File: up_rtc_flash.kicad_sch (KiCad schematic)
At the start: 12 parts, among them IC202 PCF8563T_5,518, IC203 W25Q128JVSIQTR, X201 PCIE-52P40H, X202 32.768 kHz, X203 TF-15×15, X204 CR1220-2ZX

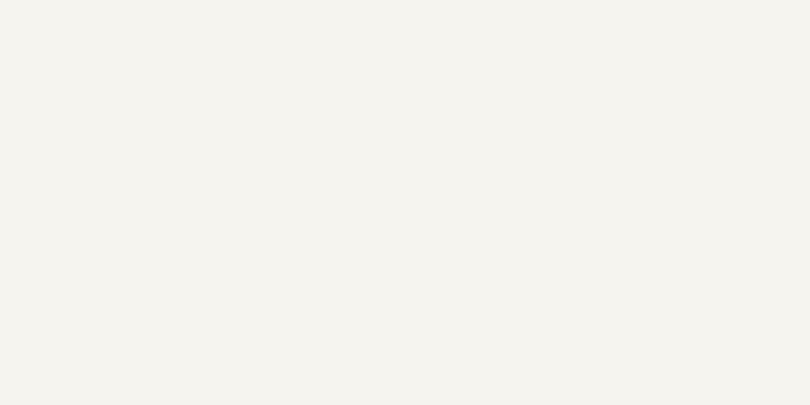
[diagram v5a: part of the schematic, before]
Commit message: add I2C0 Pullups
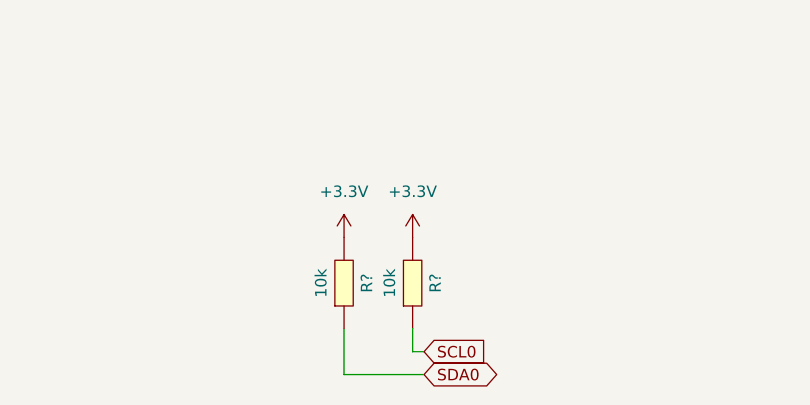
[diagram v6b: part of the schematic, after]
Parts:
- added R? (x2): 10k, R0402, symbol eduboardv2:0402WGF100JTCE
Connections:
- net SCL0: now also R?.1
- net SDA0: now also R?.1
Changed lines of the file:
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@@
   (junction (at 240.03 64.77) (diameter 0) (color 0 0 0 0)
   )
+  (wire (pts (xy 162.56 190.5) (xy 163.83 190.5))
+    (stroke (width 0) (type default) (color 0 0 0 0))
+  )
   (wire (pts (xy 168.91 39.37) (xy 171.45 39.37))
     (stroke (width 0) (type default) (color 0 0 0 0))
   )
+  (wire (pts (xy 154.94 193.04) (xy 163.83 193.04))
+    (stroke (width 0) (type default) (color 0 0 0 0))
+  )
   (wire (pts (xy 217.17 39.37) (xy 236.22 39.37))
     (stroke (width 0) (type default) (color 0 0 0 0))
@@
     (stroke (width 0) (type default) (color 0 0 0 0))
   )
+  (wire (pts (xy 162.56 187.96) (xy 162.56 190.5))
+    (stroke (width 0) (type default) (color 0 0 0 0))
+  )
   (wire (pts (xy 171.45 39.37) (xy 189.23 39.37))
     (stroke (width 0) (type default) (color 0 0 0 0))
@@
   )
   (wire (pts (xy 252.73 44.45) (xy 252.73 39.37))
+    (stroke (width 0) (type default) (color 0 0 0 0))
+  )
+  (wire (pts (xy 154.94 187.96) (xy 154.94 193.04))
     (stroke (width 0) (type default) (color 0 0 0 0))
   )
@@
     )
   )
+  (global_label "SDA0" (shape bidirectional) (at 163.83 193.04 0) (fields_autoplaced)
+    (effects (font (size 1.27 1.27)) (justify left))
+    (property "Intersheet References" "${INTERSHEET_REFS}" (id 0) (at 171.0207 192.9606 0)
+      (effects (font (size 1.27 1.27)) (justify left) hide)
+    )
+  )
+  (global_label "SCL0" (shape input) (at 163.83 190.5 0) (fields_autoplaced)
+    (effects (font (size 1.27 1.27)) (justify left))
+    (property "Intersheet References" "${INTERSHEET_REFS}" (id 0) (at 170.9602 190.4206 0)
+      (effects (font (size 1.27 1.27)) (justify left) hide)
+    )
+  )
   (global_label "RTC_INT" (shape output) (at 189.23 44.45 180) (fields_autoplaced)
     (effects (font (size 1.27 1.27)) (justify right))
@@
     (pin "1")
     (pin "2")
+  )
+  (symbol (lib_name "+3.3V_2") (lib_id "eduboardv2:+3.3V") (at 154.94 177.8 0) (unit 1)
+    (in_bom yes) (on_board yes) (fields_autoplaced)
+    (property "Reference" "#PWR?" (id 0) (at 154.94 181.61 0)
+      (effects (font (size 1.27 1.27)) hide)
+    )
+    (property "Value" "+3.3V" (id 1) (at 154.94 172.72 0))
+    (property "Footprint" "" (id 2) (at 154.94 177.8 0)
+      (effects (font (size 1.27 1.27)) hide)
+    )
+    (property "Datasheet" "" (id 3) (at 154.94 177.8 0)
+      (effects (font (size 1.27 1.27)) hide)
+    )
+    (pin "1")
   )
   (symbol (lib_name "GND_6") (lib_id "eduboardv2:GND") (at 220.98 133.35 270) (unit 1)
@@
     )
     (pin "1")
+  )
+  (symbol (lib_name "0402WGF100JTCE_10") (lib_id "eduboardv2:0402WGF100JTCE") (at 154.94 182.88 90) (unit 1)
+    (in_bom yes) (on_board yes)
+    (property "Reference" "R?" (id 0) (at 157.48 182.88 0))
+    (property "Value" "10k" (id 1) (at 152.4 182.88 0))
+    (property "Footprint" "R0402" (id 2) (at 162.56 182.88 0)
+      (effects (font (size 1.27 1.27)) hide)
+    )
+    (property "Datasheet" "https://lcsc.com/product-detail/Chip-Resistor-Surface-Mount-UniOhm_10R-10R0-1_C25077.html" (id 3) (at 167.64 182.88 0)
+      (effects (font (size 1.27 1.27)) hide)
+    )
+    (property "Manufacturer" "UniOhm" (id 4) (at 170.18 182.88 0)
+      (effects (font (size 1.27 1.27)) hide)
+    )
+    (property "LCSC Part" "C25077" (id 5) (at 172.72 182.88 0)
+      (effects (font (size 1.27 1.27)) hide)
+    )
+    (property "JLC Part" "Basic Part" (id 6) (at 175.26 182.88 0)
+      (effects (font (size 1.27 1.27)) hide)
+    )
+    (property "MPN" "0402WGF100JTCE" (id 7) (at 160.02 182.88 0)
+      (effects (font (size 1.27 1.27)) hide)
+    )
+    (pin "1")
+    (pin "2")
   )
   (symbol (lib_id "eduboardv2:+3.3V") (at 195.58 123.19 0) (unit 1)
@@
     (pin "9")
   )
+  (symbol (lib_name "0402WGF100JTCE_10") (lib_id "eduboardv2:0402WGF100JTCE") (at 162.56 182.88 90) (unit 1)
+    (in_bom yes) (on_board yes)
+    (property "Reference" "R?" (id 0) (at 165.1 182.88 0))
+    (property "Value" "10k" (id 1) (at 160.02 182.88 0))
+    (property "Footprint" "R0402" (id 2) (at 170.18 182.88 0)
+      (effects (font (size 1.27 1.27)) hide)
+    )
+    (property "Datasheet" "https://lcsc.com/product-detail/Chip-Resistor-Surface-Mount-UniOhm_10R-10R0-1_C25077.html" (id 3) (at 175.26 182.88 0)
+      (effects (font (size 1.27 1.27)) hide)
+    )
+    (property "Manufacturer" "UniOhm" (id 4) (at 177.8 182.88 0)
+      (effects (font (size 1.27 1.27)) hide)
+    )
+    (property "LCSC Part" "C25077" (id 5) (at 180.34 182.88 0)
+      (effects (font (size 1.27 1.27)) hide)
+    )
+    (property "JLC Part" "Basic Part" (id 6) (at 182.88 182.88 0)
+      (effects (font (size 1.27 1.27)) hide)
+    )
+    (property "MPN" "0402WGF100JTCE" (id 7) (at 167.64 182.88 0)
+      (effects (font (size 1.27 1.27)) hide)
+    )
+    (pin "1")
+    (pin "2")
+  )
   (symbol (lib_name "+3.3V_2") (lib_id "eduboardv2:+3.3V") (at 236.22 26.67 0) (unit 1)
     (in_bom yes) (on_board yes) (fields_autoplaced)
@@
       (effects (font (size 1.27 1.27)) hide)
     )
+    (pin "1")
+  )
+  (symbol (lib_name "+3.3V_2") (lib_id "eduboardv2:+3.3V") (at 162.56 177.8 0) (unit 1)
+    (in_bom yes) (on_board yes) (fields_autoplaced)
+    (property "Reference" "#PWR?" (id 0) (at 162.56 181.61 0)
+      (effects (font (size 1.27 1.27)) hide)
+    )
+    (property "Value" "+3.3V" (id 1) (at 162.56 172.72 0))
+    (property "Footprint" "" (id 2) (at 162.56 177.8 0)
+      (effects (font (size 1.27 1.27)) hide)
+    )
+    (property "Datasheet" "" (id 3) (at 162.56 177.8 0)
+      (effects (font (size 1.27 1.27)) hide)
+    )

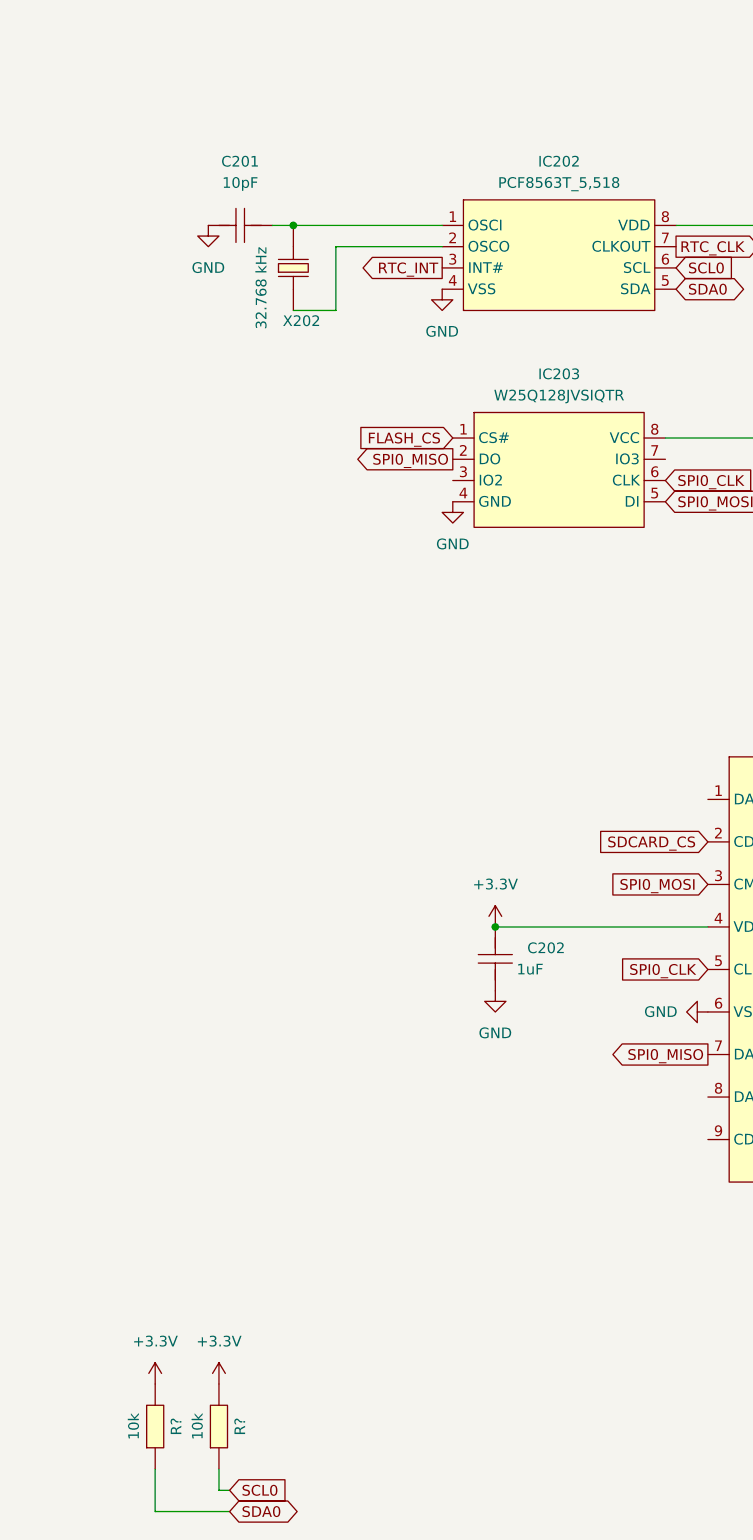
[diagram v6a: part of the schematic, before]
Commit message: reassign symbol references after page movements. Place in pcb
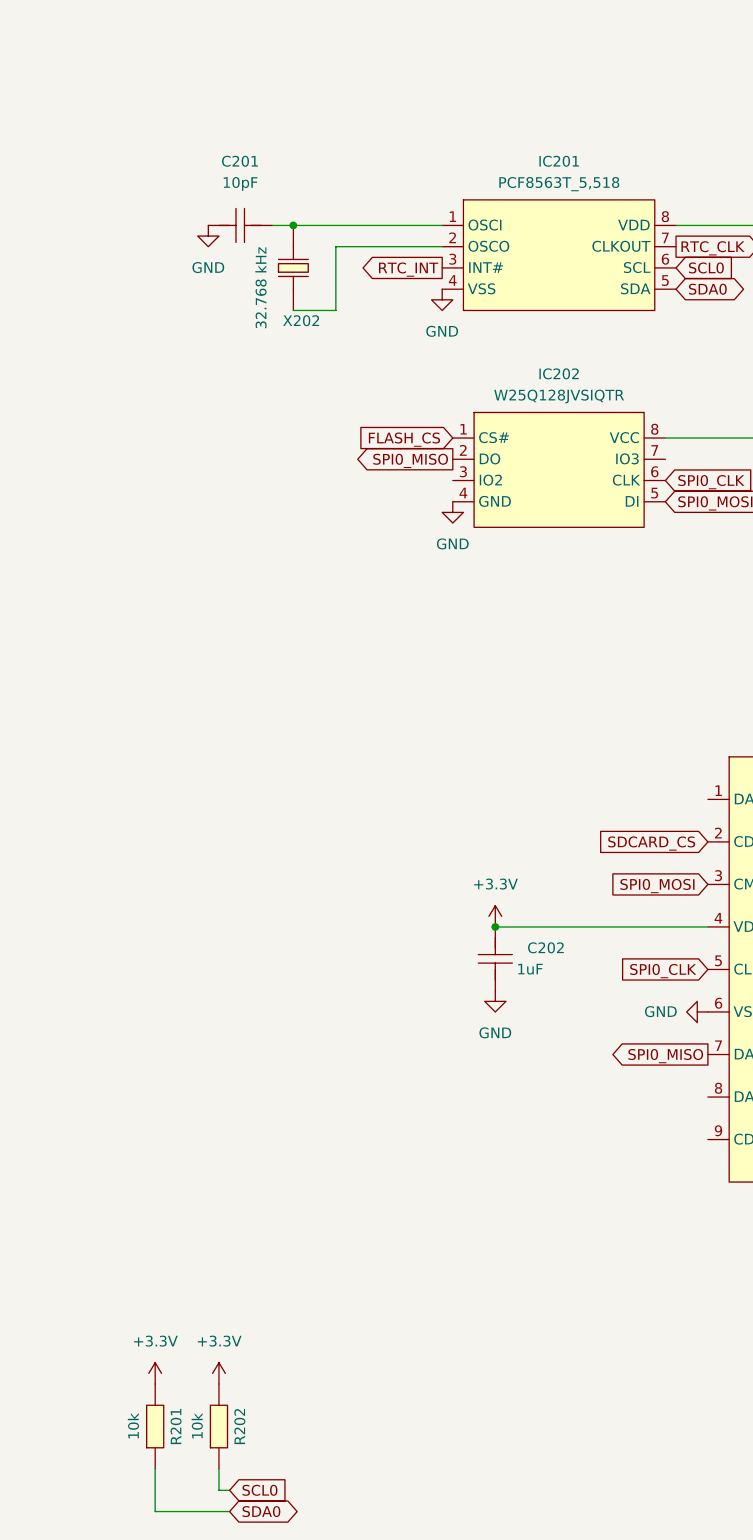
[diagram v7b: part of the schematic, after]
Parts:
- C201, C202, C203, C204: footprint C0402 -> eduboardv2:C0402
- D201, D202: footprint SOD-123_L2.7-W1.6-LS3.7-RD-1 -> eduboardv2:SOD-123_L2.7-W1.6-LS3.7-RD-1
- IC201: renamed from IC202; footprint SOIC-8_L5.0-W4.0-P1.27-LS6.0-BL -> eduboardv2:SOIC-8_L5.0-W4.0-P1.27-LS6.0-BL
- IC202: renamed from IC203; footprint SOIC-8_L5.3-W5.3-P1.27-LS8.0-BL -> eduboardv2:SOIC-8_L5.3-W5.3-P1.27-LS8.0-BL
- R201, R202: renamed from R?; footprint R0402 -> eduboardv2:R0402
- X201: footprint PCIE-SMD_PCIE-52P40H -> eduboardv2:PCIE-SMD_PCIE-52P40H
- X202: footprint FC-135R_L3.2-W1.5 -> eduboardv2:FC-135R_L3.2-W1.5
- X203: footprint TF-SMD_TF-15-15 -> eduboardv2:TF-SMD_TF-15-15
- X204: footprint BAT-SMD_CR1220-2ZX -> eduboardv2:BAT-SMD_CR1220-2ZX
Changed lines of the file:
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@@
     (property "Reference" "D202" (id 0) (at 247.269 33.02 0))
     (property "Value" "B5819W_C8598" (id 1) (at 247.269 35.56 0))
-    (property "Footprint" "SOD-123_L2.7-W1.6-LS3.7-RD-1" (id 2) (at 247.65 46.99 0)
+    (property "Footprint" "eduboardv2:SOD-123_L2.7-W1.6-LS3.7-RD-1" (id 2) (at 247.65 46.99 0)
       (effects (font (size 1.27 1.27)) hide)
     )
@@
   (symbol (lib_name "+3.3V_2") (lib_id "eduboardv2:+3.3V") (at 154.94 177.8 0) (unit 1)
     (in_bom yes) (on_board yes) (fields_autoplaced)
-    (property "Reference" "#PWR?" (id 0) (at 154.94 181.61 0)
+    (property "Reference" "#PWR0201" (id 0) (at 154.94 181.61 0)
       (effects (font (size 1.27 1.27)) hide)
     )
@@
   (symbol (lib_name "GND_6") (lib_id "eduboardv2:GND") (at 220.98 133.35 270) (unit 1)
     (in_bom yes) (on_board yes)
-    (property "Reference" "#PWR0206" (id 0) (at 214.63 133.35 0)
+    (property "Reference" "#PWR0208" (id 0) (at 214.63 133.35 0)
       (effects (font (size 1.27 1.27)) hide)
     )
@@
   (symbol (lib_id "eduboardv2:W25Q128JVSIQTR") (at 203.2 68.58 0) (unit 1)
     (in_bom yes) (on_board yes) (fields_autoplaced)
-    (property "Reference" "IC203" (id 0) (at 203.2 57.15 0))
+    (property "Reference" "IC202" (id 0) (at 203.2 57.15 0))
     (property "Value" "W25Q128JVSIQTR" (id 1) (at 203.2 59.69 0))
-    (property "Footprint" "SOIC-8_L5.3-W5.3-P1.27-LS8.0-BL" (id 2) (at 203.2 80.01 0)
+    (property "Footprint" "eduboardv2:SOIC-8_L5.3-W5.3-P1.27-LS8.0-BL" (id 2) (at 203.2 80.01 0)
       (effects (font (size 1.27 1.27)) hide)
     )
@@
   (symbol (lib_name "GND_2") (lib_id "eduboardv2:GND") (at 190.5 72.39 0) (unit 1)
     (in_bom yes) (on_board yes) (fields_autoplaced)
-    (property "Reference" "#PWR0203" (id 0) (at 190.5 78.74 0)
+    (property "Reference" "#PWR0205" (id 0) (at 190.5 78.74 0)
       (effects (font (size 1.27 1.27)) hide)
     )
@@
     (property "Reference" "C201" (id 0) (at 165.1 31.75 0))
     (property "Value" "10pF" (id 1) (at 165.1 34.29 0))
-    (property "Footprint" "C0402" (id 2) (at 165.1 31.75 0)
+    (property "Footprint" "eduboardv2:C0402" (id 2) (at 165.1 31.75 0)
       (effects (font (size 1.27 1.27)) hide)
     )
@@
       (effects (font (size 1.27 1.27)) (justify right))
     )
-    (property "Footprint" "C0402" (id 2) (at 243.84 43.18 0)
+    (property "Footprint" "eduboardv2:C0402" (id 2) (at 243.84 43.18 0)
       (effects (font (size 1.27 1.27)) hide)
     )
@@
       (effects (font (size 1.27 1.27)) (justify left))
     )
-    (property "Footprint" "BAT-SMD_CR1220-2ZX" (id 2) (at 245.11 48.26 0)
+    (property "Footprint" "eduboardv2:BAT-SMD_CR1220-2ZX" (id 2) (at 245.11 48.26 0)
       (effects (font (size 1.27 1.27)) hide)
     )
@@
   (symbol (lib_name "GND_3") (lib_id "eduboardv2:GND") (at 189.23 46.99 0) (unit 1)
     (in_bom yes) (on_board yes) (fields_autoplaced)
-    (property "Reference" "#PWR0202" (id 0) (at 189.23 53.34 0)
+    (property "Reference" "#PWR0204" (id 0) (at 189.23 53.34 0)
       (effects (font (size 1.27 1.27)) hide)
     )
@@
       (effects (font (size 1.27 1.27)) (justify right))
     )
-    (property "Footprint" "C0402" (id 2) (at 203.2 127 0)
+    (property "Footprint" "eduboardv2:C0402" (id 2) (at 203.2 127 0)
       (effects (font (size 1.27 1.27)) hide)
     )
@@
       (effects (font (size 1.27 1.27)) (justify right))
     )
-    (property "Footprint" "SOD-123_L2.7-W1.6-LS3.7-RD-1" (id 2) (at 243.84 30.48 0)
+    (property "Footprint" "eduboardv2:SOD-123_L2.7-W1.6-LS3.7-RD-1" (id 2) (at 243.84 30.48 0)
       (effects (font (size 1.27 1.27)) hide)
     )
@@
   (symbol (lib_name "+3.3V_1") (lib_id "eduboardv2:+3.3V") (at 240.03 64.77 0) (unit 1)
     (in_bom yes) (on_board yes) (fields_autoplaced)
-    (property "Reference" "#PWR0209" (id 0) (at 240.03 68.58 0)
+    (property "Reference" "#PWR0211" (id 0) (at 240.03 68.58 0)
       (effects (font (size 1.27 1.27)) hide)
     )
@@
   (symbol (lib_name "0402WGF100JTCE_10") (lib_id "eduboardv2:0402WGF100JTCE") (at 154.94 182.88 90) (unit 1)
     (in_bom yes) (on_board yes)
-    (property "Reference" "R?" (id 0) (at 157.48 182.88 0))
+    (property "Reference" "R201" (id 0) (at 157.48 182.88 0))
     (property "Value" "10k" (id 1) (at 152.4 182.88 0))
-    (property "Footprint" "R0402" (id 2) (at 162.56 182.88 0)
+    (property "Footprint" "eduboardv2:R0402" (id 2) (at 162.56 182.88 0)
       (effects (font (size 1.27 1.27)) hide)
     )
@@
   (symbol (lib_id "eduboardv2:+3.3V") (at 195.58 123.19 0) (unit 1)
     (in_bom yes) (on_board yes) (fields_autoplaced)
-    (property "Reference" "#PWR0204" (id 0) (at 195.58 127 0)
+    (property "Reference" "#PWR0206" (id 0) (at 195.58 127 0)
       (effects (font (size 1.27 1.27)) hide)
     )
@@
   (symbol (lib_name "GND_1") (lib_id "eduboardv2:GND") (at 161.29 39.37 0) (unit 1)
     (in_bom yes) (on_board yes) (fields_autoplaced)
-    (property "Reference" "#PWR0201" (id 0) (at 161.29 45.72 0)
+    (property "Reference" "#PWR0202" (id 0) (at 161.29 45.72 0)
       (effects (font (size 1.27 1.27)) hide)
     )
@@
       (effects (font (size 1.27 1.27)) (justify left))
     )
-    (property "Footprint" "PCIE-SMD_PCIE-52P40H" (id 2) (at 40.64 71.12 0)
+    (property "Footprint" "eduboardv2:PCIE-SMD_PCIE-52P40H" (id 2) (at 40.64 71.12 0)
       (effects (font (size 1.27 1.27)) hide)
     )
@@
       (effects (font (size 1.27 1.27)) (justify left))
     )
-    (property "Footprint" "TF-SMD_TF-15-15" (id 2) (at 240.03 163.83 0)
+    (property "Footprint" "eduboardv2:TF-SMD_TF-15-15" (id 2) (at 240.03 163.83 0)
       (effects (font (size 1.27 1.27)) hide)
     )
@@
   (symbol (lib_name "0402WGF100JTCE_10") (lib_id "eduboardv2:0402WGF100JTCE") (at 162.56 182.88 90) (unit 1)
     (in_bom yes) (on_board yes)
-    (property "Reference" "R?" (id 0) (at 165.1 182.88 0))
+    (property "Reference" "R202" (id 0) (at 165.1 182.88 0))
     (property "Value" "10k" (id 1) (at 160.02 182.88 0))
-    (property "Footprint" "R0402" (id 2) (at 170.18 182.88 0)
+    (property "Footprint" "eduboardv2:R0402" (id 2) (at 170.18 182.88 0)
       (effects (font (size 1.27 1.27)) hide)
     )
@@
   (symbol (lib_name "+3.3V_2") (lib_id "eduboardv2:+3.3V") (at 236.22 26.67 0) (unit 1)
     (in_bom yes) (on_board yes) (fields_autoplaced)
-    (property "Reference" "#PWR0207" (id 0) (at 236.22 30.48 0)
+    (property "Reference" "#PWR0209" (id 0) (at 236.22 30.48 0)
       (effects (font (size 1.27 1.27)) hide)
     )
@@
   (symbol (lib_name "GND_5") (lib_id "eduboardv2:GND") (at 240.03 72.39 0) (unit 1)
     (in_bom yes) (on_board yes) (fields_autoplaced)
-    (property "Reference" "#PWR0210" (id 0) (at 240.03 78.74 0)
+    (property "Reference" "#PWR0212" (id 0) (at 240.03 78.74 0)
       (effects (font (size 1.27 1.27)) hide)
     )
@@
       (effects (font (size 1.27 1.27)) (justify right))
     )
-    (property "Footprint" "FC-135R_L3.2-W1.5" (id 2) (at 179.07 44.45 0)
+    (property "Footprint" "eduboardv2:FC-135R_L3.2-W1.5" (id 2) (at 179.07 44.45 0)
       (effects (font (size 1.27 1.27)) hide)
     )
@@
       (effects (font (size 1.27 1.27)) (justify right))
     )
-    (property "Footprint" "C0402" (id 2) (at 247.65 68.58 0)
+    (property "Footprint" "eduboardv2:C0402" (id 2) (at 247.65 68.58 0)
       (effects (font (size 1.27 1.27)) hide)
     )
@@
   (symbol (lib_name "GND_7") (lib_id "eduboardv2:GND") (at 252.73 52.07 0) (unit 1)
     (in_bom yes) (on_board yes) (fields_autoplaced)
-    (property "Reference" "#PWR0211" (id 0) (at 252.73 58.42 0)
+    (property "Reference" "#PWR0213" (id 0) (at 252.73 58.42 0)
       (effects (font (size 1.27 1.27)) hide)
     )
@@
   (symbol (lib_name "+3.3V_2") (lib_id "eduboardv2:+3.3V") (at 162.56 177.8 0) (unit 1)
     (in_bom yes) (on_board yes) (fields_autoplaced)
-    (property "Reference" "#PWR?" (id 0) (at 162.56 181.61 0)
+    (property "Reference" "#PWR0203" (id 0) (at 162.56 181.61 0)
       (effects (font (size 1.27 1.27)) hide)
     )
@@
   (symbol (lib_id "eduboardv2:PCF8563T_5,518") (at 203.2 43.18 0) (unit 1)
     (in_bom yes) (on_board yes) (fields_autoplaced)
-    (property "Reference" "IC202" (id 0) (at 203.2 31.75 0))
+    (property "Reference" "IC201" (id 0) (at 203.2 31.75 0))
     (property "Value" "PCF8563T_5,518" (id 1) (at 203.2 34.29 0))
-    (property "Footprint" "SOIC-8_L5.0-W4.0-P1.27-LS6.0-BL" (id 2) (at 203.2 54.61 0)
+    (property "Footprint" "eduboardv2:SOIC-8_L5.0-W4.0-P1.27-LS6.0-BL" (id 2) (at 203.2 54.61 0)
       (effects (font (size 1.27 1.27)) hide)
     )
@@
   (symbol (lib_id "eduboardv2:GND") (at 195.58 130.81 0) (unit 1)
     (in_bom yes) (on_board yes) (fields_autoplaced)
-    (property "Reference" "#PWR0205" (id 0) (at 195.58 137.16 0)
+    (property "Reference" "#PWR0207" (id 0) (at 195.58 137.16 0)
       (effects (font (size 1.27 1.27)) hide)
     )
@@
   (symbol (lib_name "GND_4") (lib_id "eduboardv2:GND") (at 236.22 46.99 0) (unit 1)
     (in_bom yes) (on_board yes) (fields_autoplaced)
-    (property "Reference" "#PWR0208" (id 0) (at 236.22 53.34 0)
-      (effects (font (size 1.27 1.27)) hide)
-    )
+    (property "Reference" "#PWR0210" (id 0) (at 236.22 53.34 0)
+      (effects (font (size 1.27 1.27)) hide)
+    )
